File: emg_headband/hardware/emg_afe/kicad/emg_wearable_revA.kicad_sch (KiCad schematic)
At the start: 63 parts, among them J1 CH1 (TRS), J3 LiPo pads (protected cell), J6 FLEX ARRAY CH1-3 (FPC 12P 0.5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, J7 USB-C, Q101 AO3401A, U1 ADS1298IPAGR, U2 ESP32-S3-MINI-1-N8, U6 LP5907MFX-3.0, U7 USBLC6-2SC6, U8 MCP73831T-2ACI/OT, U9 AP2112K-3.3TRG1

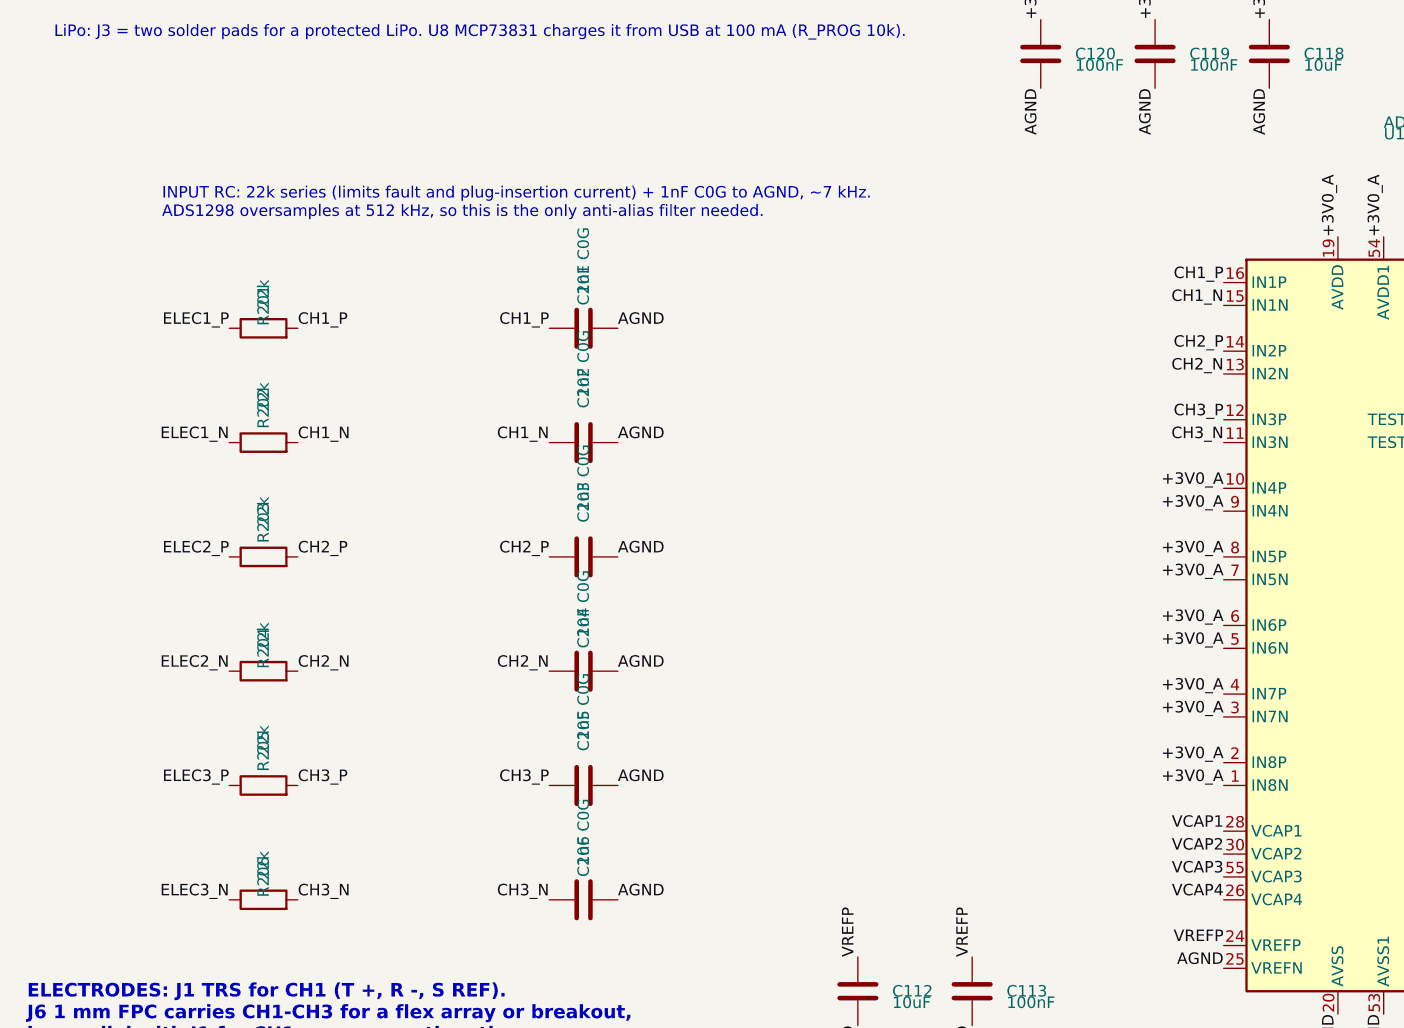
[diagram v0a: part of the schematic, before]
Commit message: EMG Rev A: input caps 1 nF -> 100 pF C0G for dry-electrode CMRR
Co-Authored-By: Claude Opus 5.5 (1M context) <noreply@anthropic.com>
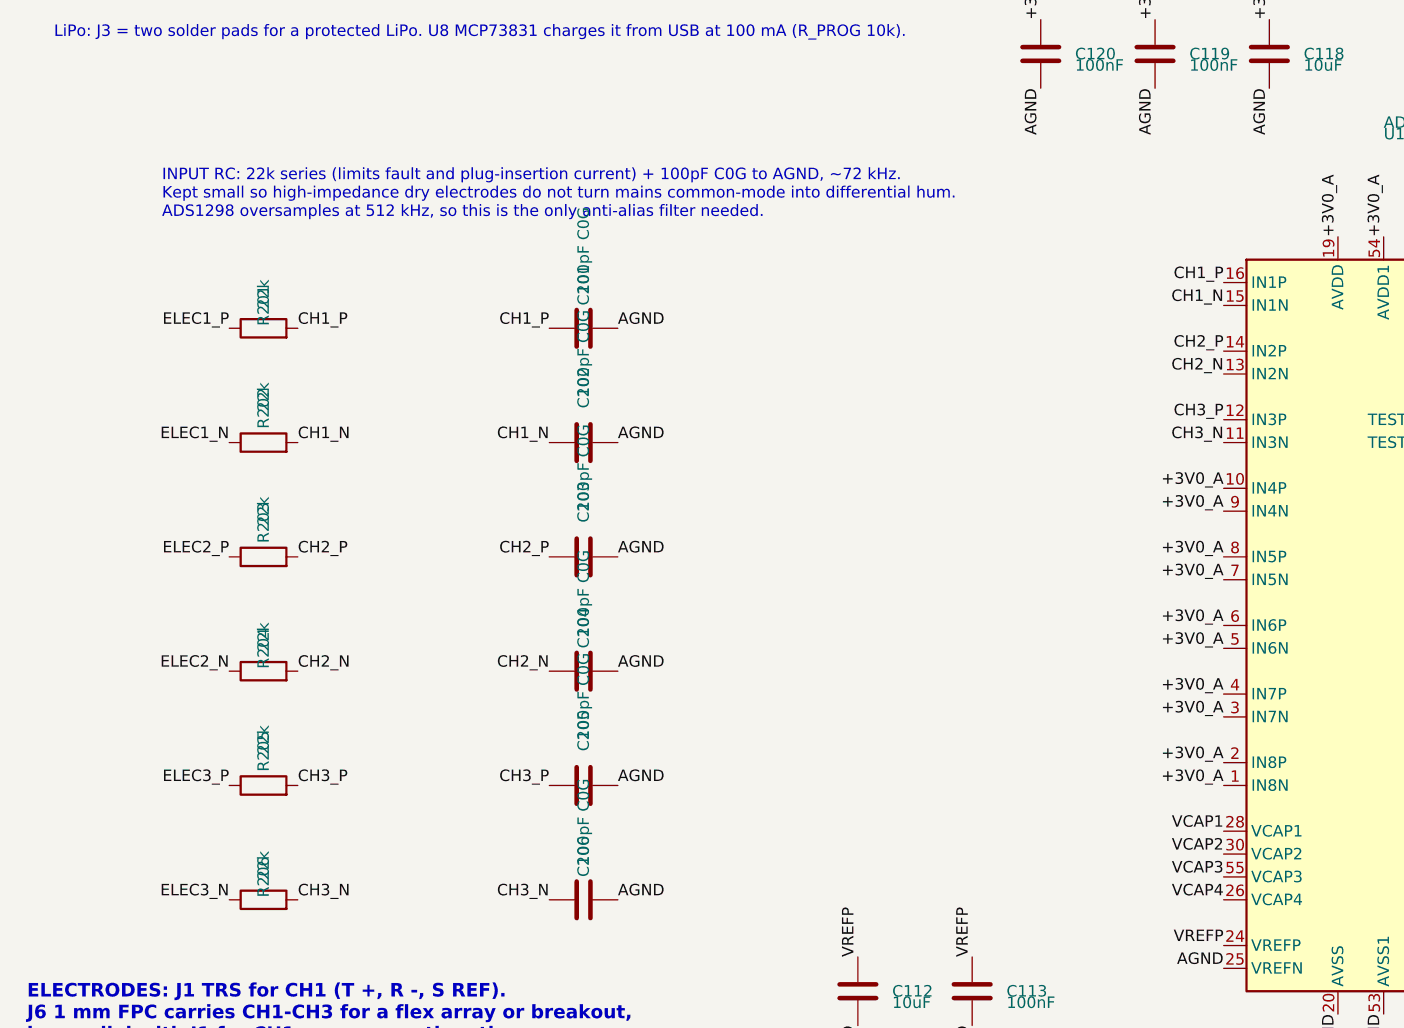
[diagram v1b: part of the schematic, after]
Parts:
- C201, C202, C203, C204, C205, C206: value 1nF C0G -> 100pF C0G; LCSC C163508 -> C14858
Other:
- note added: "INPUT RC: 22k series (limits fault and plug-insertion current) + 100pF C0G to AGND, ~72 kHz. Kept small so high-impedance dry electrodes do not turn mains common-mode into differential hum. ADS1298 oversamples at 512 kHz, so this is the only anti-alias filter needed."
- note removed: "INPUT RC: 22k series (limits fault and plug-insertion current) + 1nF C0G to AGND, ~7 kHz. ADS1298 oversamples at 512 kHz, so this is the only anti-alias filter needed."
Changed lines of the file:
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@@
 			)
 		)
-		(property "Value" "1nF C0G"
+		(property "Value" "100pF C0G"
 			(at 116.84 128.26999999999998 0)
 			(show_name no)
@@
 			)
 		)
-		(property "LCSC" "C163508"
+		(property "LCSC" "C14858"
 			(at 116.84 132.08 0)
 			(effects
@@
 			)
 		)
-		(property "Value" "1nF C0G"
+		(property "Value" "100pF C0G"
 			(at 116.84 139.7 0)
 			(show_name no)
@@
 			)
 		)
-		(property "LCSC" "C163508"
+		(property "LCSC" "C14858"
 			(at 116.84 144.78 0)
 			(effects
@@
 			)
 		)
-		(property "Value" "1nF C0G"
+		(property "Value" "100pF C0G"
 			(at 116.84 152.39999999999998 0)
 			(show_name no)
@@
 			)
 		)
-		(property "LCSC" "C163508"
+		(property "LCSC" "C14858"
 			(at 116.84 157.48 0)
 			(effects
@@
 			)
 		)
-		(property "Value" "1nF C0G"
+		(property "Value" "100pF C0G"
 			(at 116.84 166.36999999999998 0)
 			(show_name no)
@@
 			)
 		)
-		(property "LCSC" "C163508"
+		(property "LCSC" "C14858"
 			(at 116.84 170.18 0)
 			(effects
@@
 			)
 		)
-		(property "Value" "1nF C0G"
+		(property "Value" "100pF C0G"
 			(at 116.84 177.79999999999998 0)
 			(show_name no)
@@
 			)
 		)
-		(property "LCSC" "C163508"
+		(property "LCSC" "C14858"
 			(at 116.84 182.88 0)
 			(effects
@@
 			)
 		)
-		(property "Value" "1nF C0G"
+		(property "Value" "100pF C0G"
 			(at 116.84 191.76999999999998 0)
 			(show_name no)
@@
 			)
 		)
-		(property "LCSC" "C163508"
+		(property "LCSC" "C14858"
 			(at 116.84 195.58 0)
 			(effects
@@
 		)
 	)
-	(text "INPUT RC: 22k series (limits fault and plug-insertion current) + 1nF C0G to AGND, ~7 kHz.\nADS1298 oversamples at 512 kHz, so this is the only anti-alias filter needed."
+	(text "INPUT RC: 22k series (limits fault and plug-insertion current) + 100pF C0G to AGND, ~72 kHz.\nKept small so high-impedance dry electrodes do not turn mains common-mode into differential hum.\nADS1298 oversamples at 512 kHz, so this is the only anti-alias filter needed."
 		(exclude_from_sim no)
 		(at 70 120 0)

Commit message: EMG Rev A: power slide switch, battery monitor and charge LED
SW1 (MSK12C02, side lever at the bottom edge) between the battery and
the Q101 system path: off disconnects the cell, USB still powers the
board and charges. VBAT_SYS/2 divider into IO10, MCP73831 STAT LED.
Re-routed, pours and stitching redone; stiffener now covers the switch
and has holes at every peg and USB-C shell tab. ERC 0 errors, DRC 0
errors, 0 unconnected. JLC BOM/CPL (60 parts) and gerbers re-exported
with the rotation/offset corrections.

Co-Authored-By: Claude Opus 5.5 (1M context) <noreply@anthropic.com>
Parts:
- added C709: 100nF, Capacitor_SMD:C_0603_1608Metric, symbol Device:C
- added D102: CHG red, LED_SMD:LED_0603_1608Metric, symbol Device:LED
- added R705, R706: 1M, Resistor_SMD:R_0603_1608Metric, symbol Device:R
- added R707: 1k, Resistor_SMD:R_0603_1608Metric, symbol Device:R
- added SW1: PWR (MSK12C02), emg_wearable:SW_SPDT_Slide_SHOUHAN_MSK12C02, symbol Switch:SW_SPDT
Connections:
- net AGND: now also C709.2, R706.2
- net VBAT: now also SW1.2 (B); no longer Q101.3 (D)
- net VBUS: now also R707.1
- net CHG_STAT: now reaches U8.1 (STAT)
- net CHG_STAT: now also D102.1 (K)
- net VBAT_SENSE: now reaches U2.14 (IO10)
- net VBAT_SENSE: now also C709.1, R705.2, R706.1
- new net CHG_LED: D102.2 (A), R707.2
- new net VBAT_SYS: Q101.3 (D), R705.1, SW1.1 (A)
- no-connect marks 43 -> 42
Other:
- note added: "ON/OFF: SW1 disconnects the battery from the system path (Q101). Off = 0 uA from the cell; USB still powers the board and U8 still charges the cell. Slider toward pin 1 = ON (connects 2-1). BATTERY MONITOR: VBAT_SYS / 2 into IO10 (ADC1_CH9), 1M/1M + 100nF, 2 uA only while ON. CHARGE LED: D102 lit while U8 is charging (STAT low); off when full or no USB."
